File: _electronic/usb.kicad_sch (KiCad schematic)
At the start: 8 parts

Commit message: BETA first upload
nothing major done here:
* updated KiCAD files to v9
* removed alternative 6v feed-in. The proposed buck converter is fine.
* added to all components LCSC component IDs. With this, exporting the project as gerber files also automatically creates correct BOM for JLCPCB manufacturing
*
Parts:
- D_USB1: LCSC (none) -> C2290
- FB_USB1: LCSC (none) -> C369522
- F_USB1: LCSC (none) -> C269105
- J_USB1: LCSC (none) -> C2765186
- R_USB1, R_USB2: LCSC (none) -> C23186
- R_USB3: LCSC (none) -> C22975
- U_USB1: LCSC (none) -> C10508
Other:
- title: E-TKT v1.0 -> E-TKT v2.0 BETA

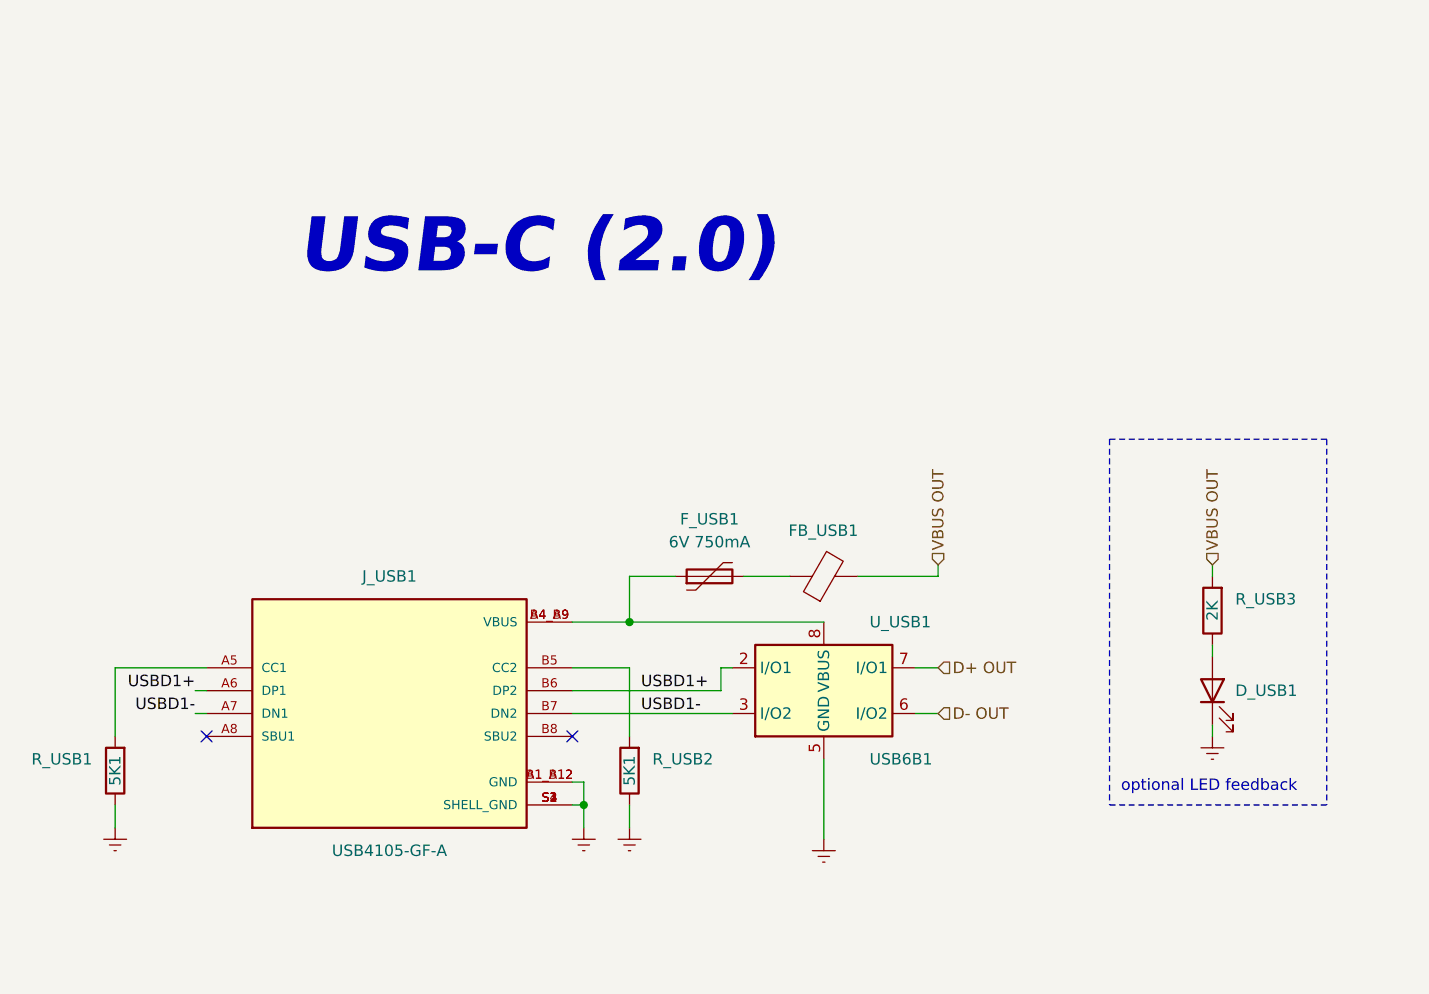
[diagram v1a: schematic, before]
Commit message: Added CAD, cleaned up KiCAD some more
Added a FreeCAD Assembly. This will serve for minor updated to the printable parts.
Updated USB-C component to standard KiCAD libary-integrated version, because the pinout of the schematic symbol was messing with the pinout of the footprint
exported the PCB as step so it could be imported to FreeCAD
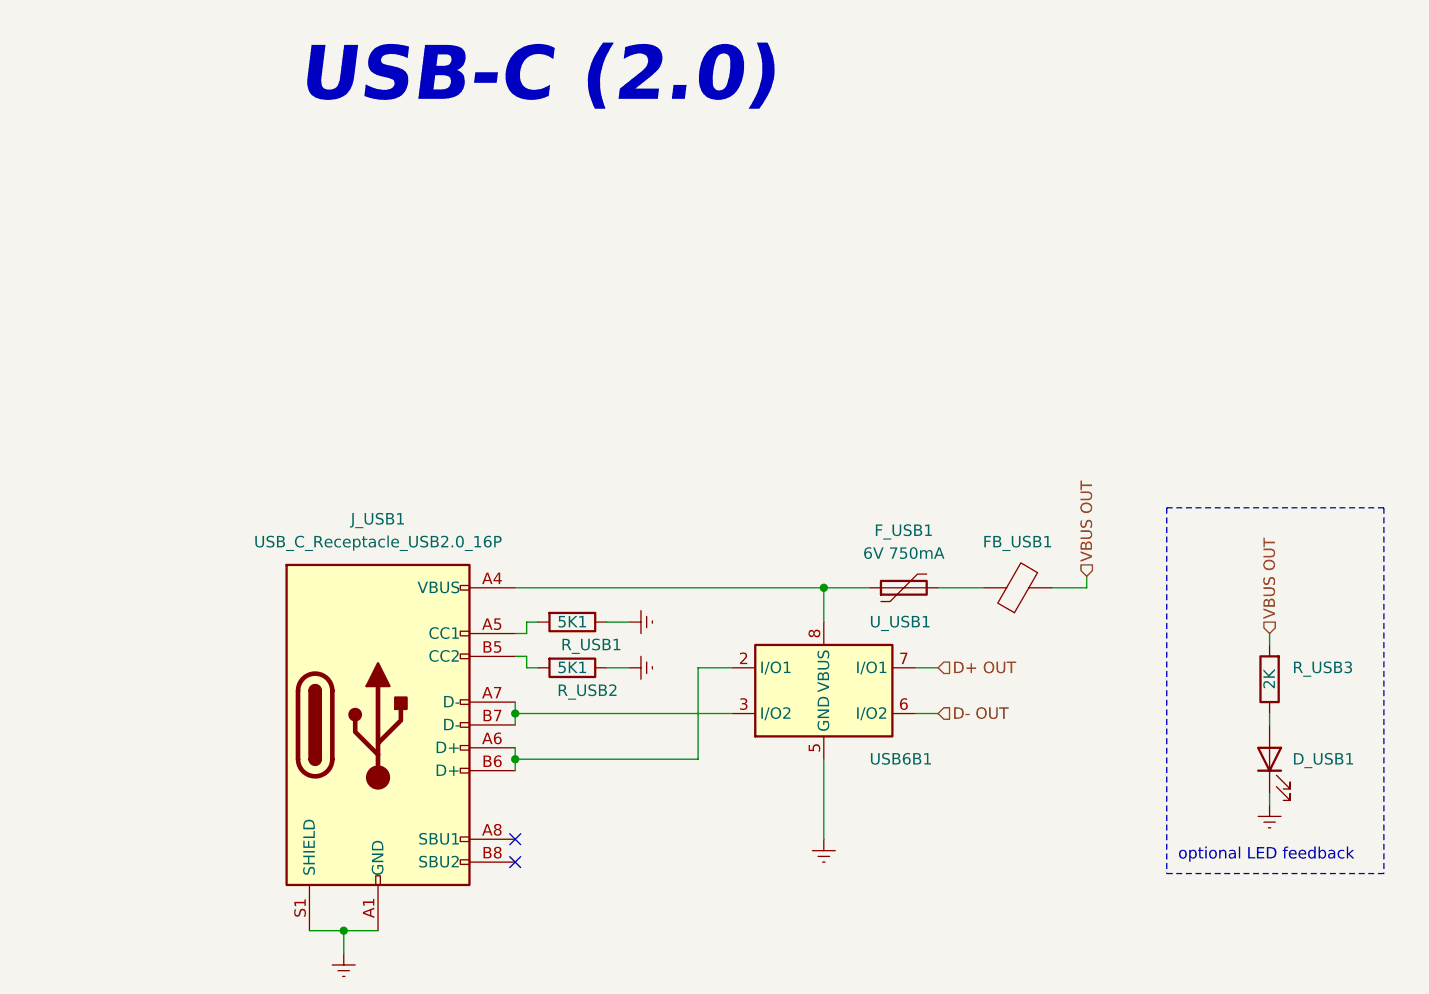
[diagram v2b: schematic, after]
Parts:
- removed J_USB1: USB4105-GF-A, SnapEDA Library:GCT_USB4105-GF-A, symbol USB4105-GF-A:USB4105-GF-A
- added J_USB1: USB_C_Receptacle_USB2.0_16P, Connector_USB:USB_C_Receptacle_GCT_USB4105-xx-A_16P_TopMnt_Horizontal, symbol Connector:USB_C_Receptacle_USB2.0_16P
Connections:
- net GNDREF: now also J_USB1.A1 (GND), J_USB1.A12 (GND), J_USB1.B1 (GND), J_USB1.B12 (GND), J_USB1.S1 (SHIELD)
- net at R_USB2.2: now also J_USB1.B5 (CC2)
- net at F_USB1.1, U_USB1.1 (VBUS), U_USB1.8 (VBUS): now also J_USB1.A4 (VBUS), J_USB1.A9 (VBUS), J_USB1.B4 (VBUS), J_USB1.B9 (VBUS)
- net at R_USB1.2: now also J_USB1.A5 (CC1)
- net USBD1+: no longer names the net of U_USB1.2 (I/O1)
- net USBD1+: now also J_USB1.A6 (D+), J_USB1.B6 (D+)
- net USBD1-: no longer names the net of U_USB1.3 (I/O2)
- net USBD1-: now also J_USB1.A7 (D-), J_USB1.B7 (D-)
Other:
- moved on the sheet: D_USB1, FB_USB1, F_USB1, R_USB1, R_USB2, R_USB3

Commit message: Added endstop
added footprint for a microswitch with roller as enstop. updated the CAD correspondingly by adding M4 hole in the nema wheel hub for an M4 12mm/16mm set screw (the ones with a pointy end).
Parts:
- J_USB1: footprint Connector_USB:USB_C_Receptacle_GCT_USB4105-xx-A_16P_TopMnt_Horizontal -> EASYEDA2KICAD:USB-TH_GT-USB-7057A
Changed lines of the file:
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@@
 			)
 		)
-		(property "Footprint" "Connector_USB:USB_C_Receptacle_GCT_USB4105-xx-A_16P_TopMnt_Horizontal"
+		(property "Footprint" "EASYEDA2KICAD:USB-TH_GT-USB-7057A"
 			(at 124.46 104.14 0)
 			(effects

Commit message: sturdyfy E-TKT
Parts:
- J_USB1: symbol Connector:USB_C_Receptacle_USB2.0_16P -> EASYEDA2KICAD:USB_C_Receptacle_USB2.0_8P
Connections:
- net GNDREF: no longer J_USB1.A12 (GND), J_USB1.B1 (GND), J_USB1.B12 (GND)
- net at F_USB1.1, J_USB1.A4 (VBUS), U_USB1.1 (VBUS)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: no longer J_USB1.A9 (VBUS), J_USB1.B4 (VBUS), J_USB1.B9 (VBUS)
- net at J_USB1.A6 (D+), U_USB1.2 (I/O1): no longer J_USB1.B6 (D+)
- net at J_USB1.A7 (D-), U_USB1.3 (I/O2): no longer J_USB1.B7 (D-)
- no-connect marks 2 -> 0
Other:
- moved on the sheet: FB_USB1, F_USB1, R_USB1, R_USB2

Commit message: JLC export added, LCSC numbers updated
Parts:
- J_USB1: LCSC (none) -> C22383830
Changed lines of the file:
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@@
+			)
+		)
+		(property "LCSC" "C22383830"
+			(at 120.65 105.41 0)
+			(effects
+				(font
+					(size 1.27 1.27)
+				)
+				(hide yes)
 			)
 		)
